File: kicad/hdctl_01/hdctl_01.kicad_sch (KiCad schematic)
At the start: 15 parts, among them J1 DIN41612_02x32_AC, J2 Conn_02x20_Odd_Even, SW1 SW_DIP_x04, U1 PAL20RS10, U2 74HCT574, U3 74HCT574, U4 74HC245, U5 74HC193

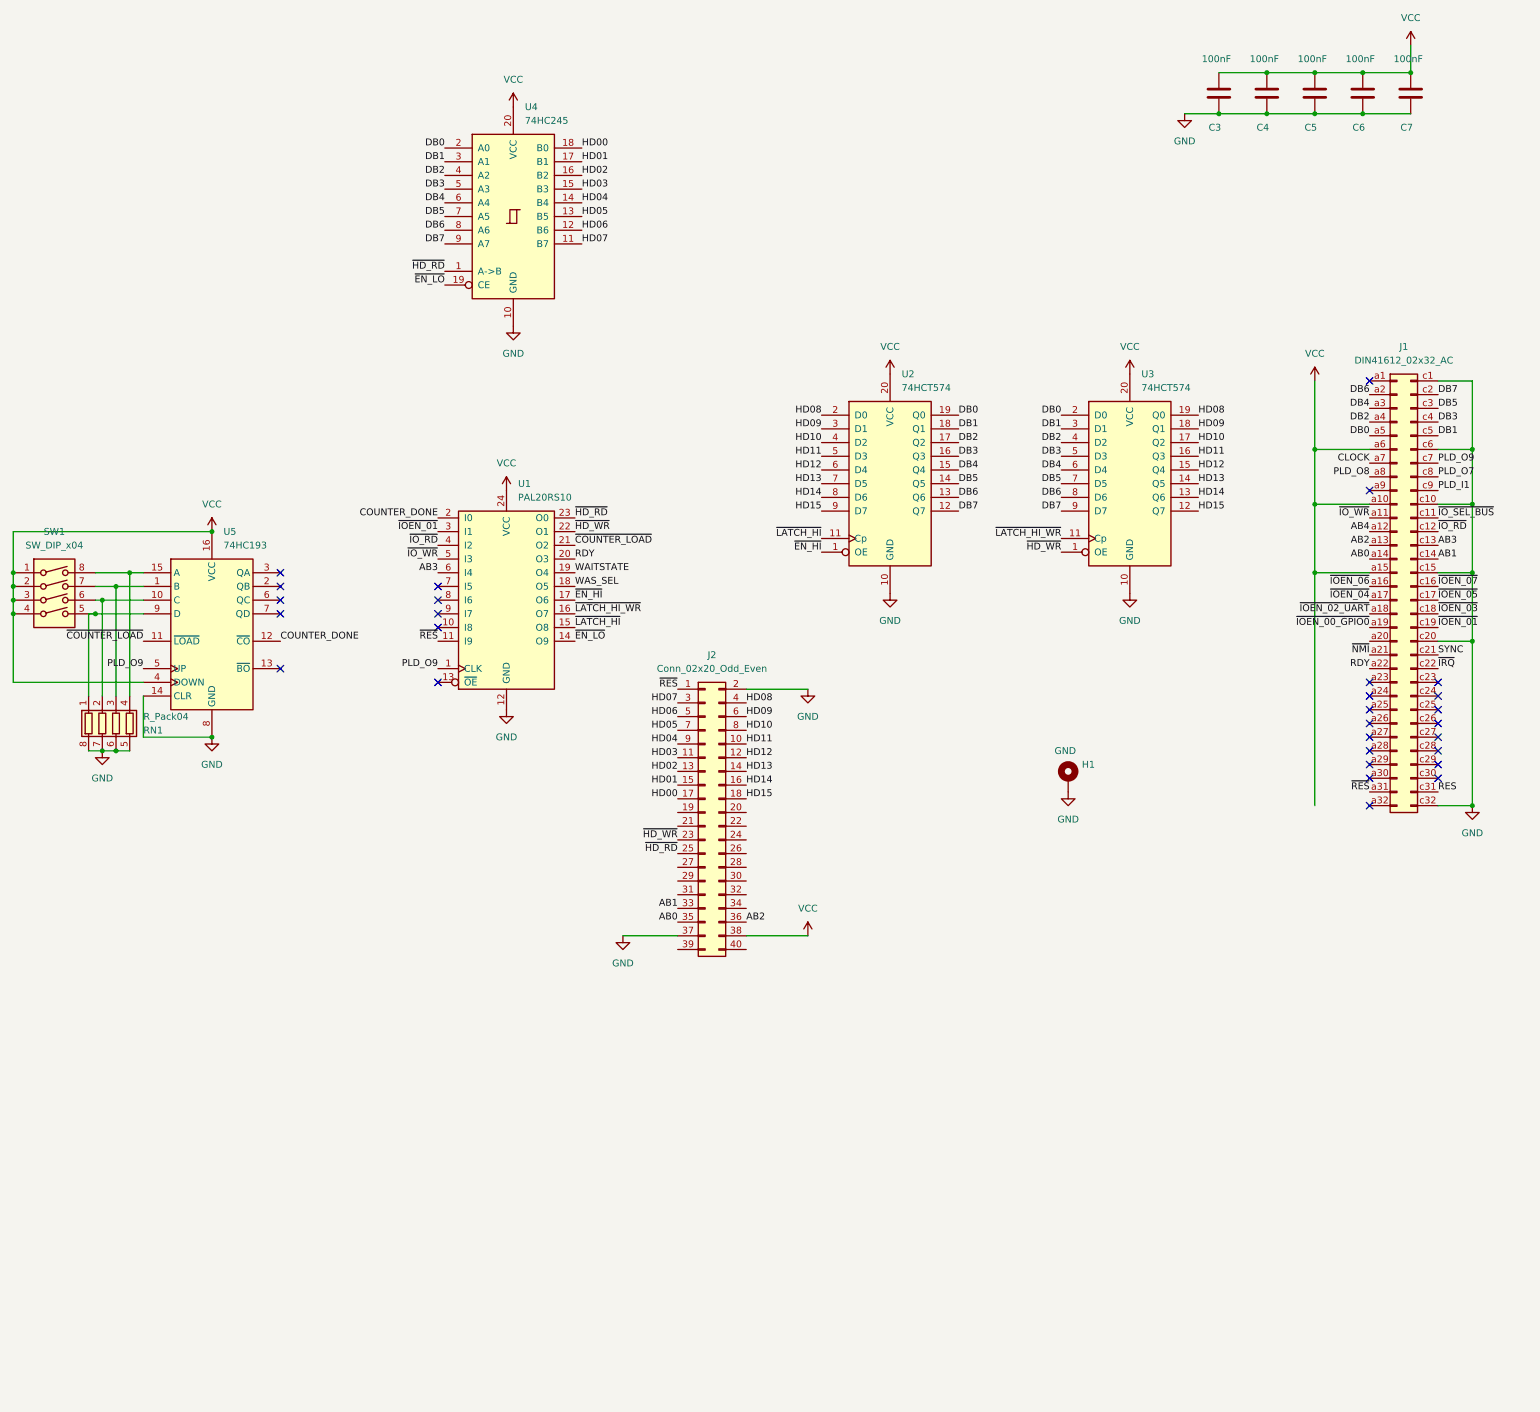
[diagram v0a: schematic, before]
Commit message: hd controller rework. should be ready for mfg (need final check)
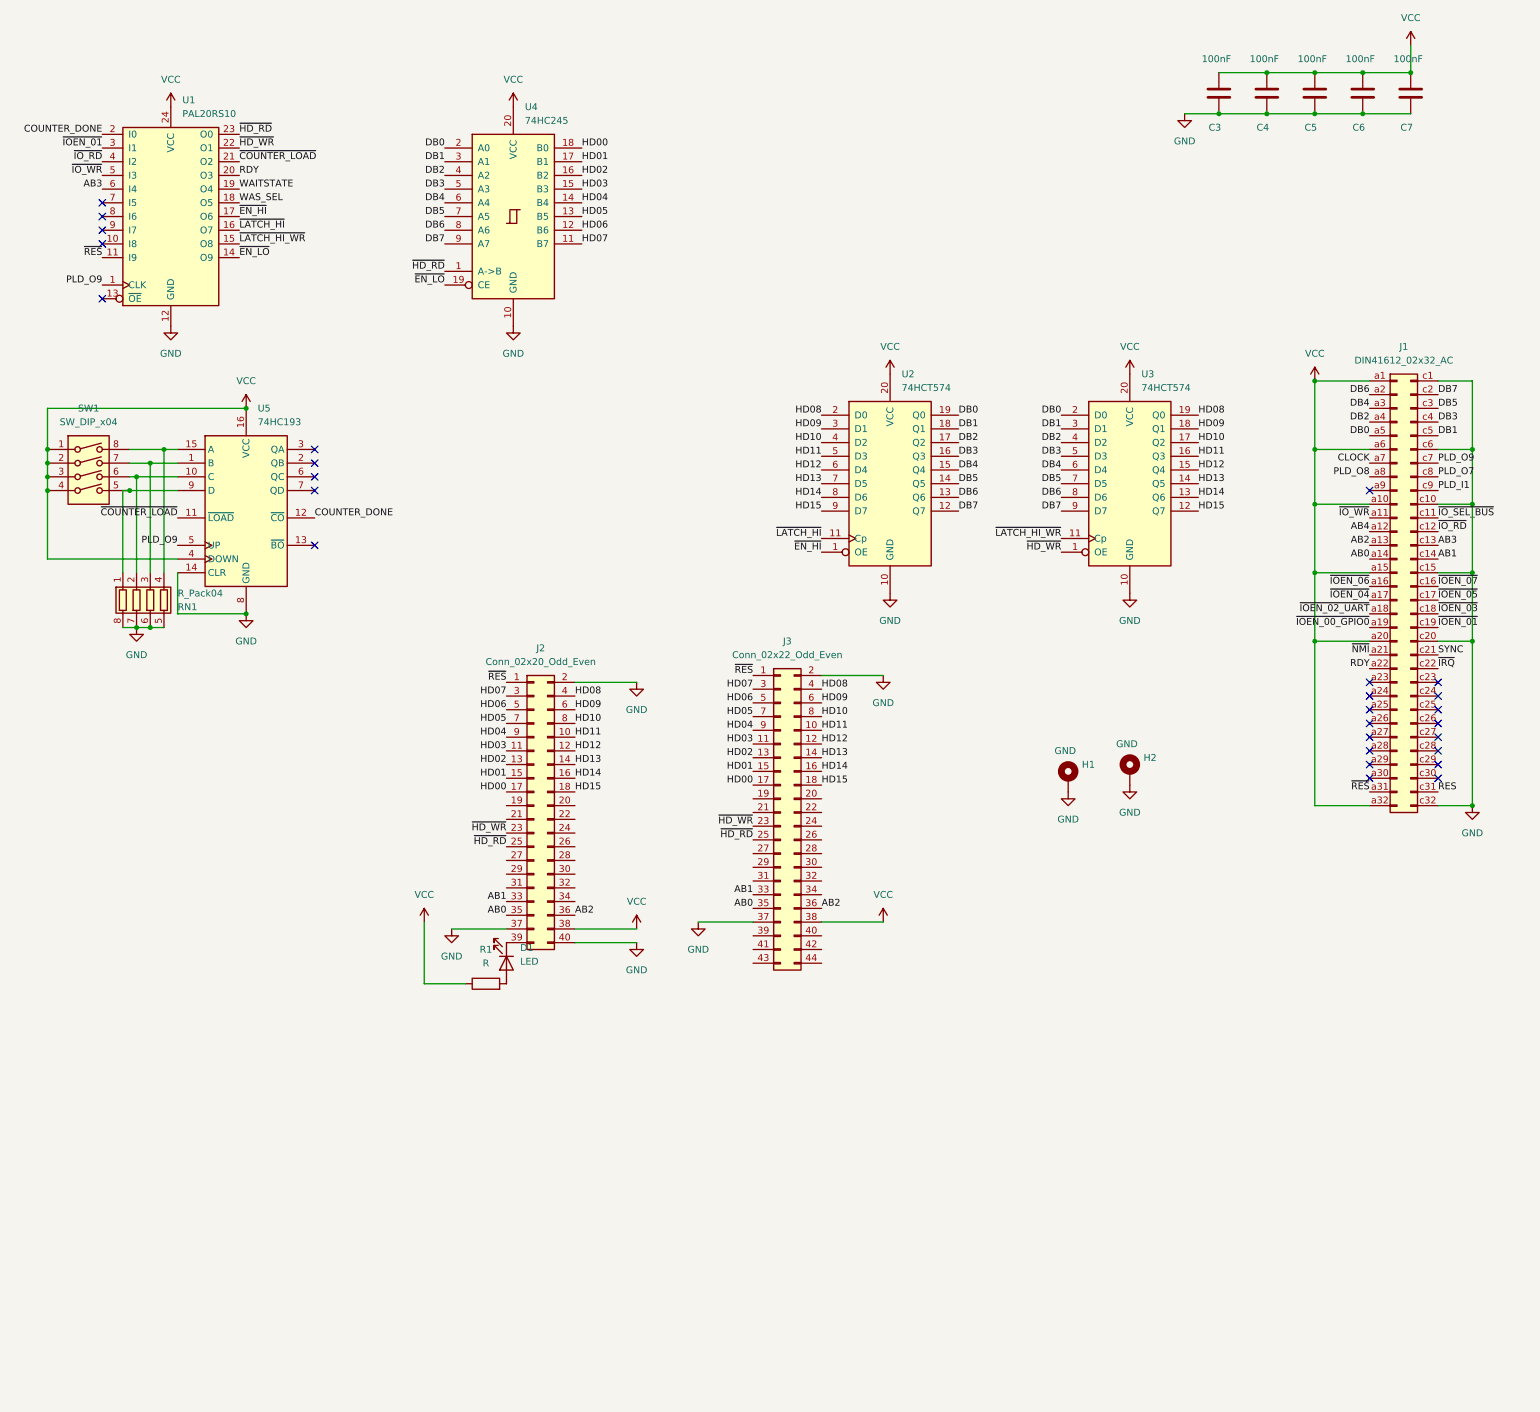
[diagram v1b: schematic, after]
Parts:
- added D1: LED, LED_SMD:LED_0805_2012Metric_Pad1.15x1.40mm_HandSolder, symbol Device:LED
- added H2: GND, MountingHole:MountingHole_3.2mm_M3_DIN965_Pad, symbol Mechanical:MountingHole_Pad
- added J3: Conn_02x22_Odd_Even, Connector_PinSocket_2.00mm:PinSocket_2x22_P2.00mm_Horizontal, symbol Connector_Generic:Conn_02x22_Odd_Even
- added R1: R, Resistor_SMD:R_0805_2012Metric_Pad1.20x1.40mm_HandSolder, symbol Device:R
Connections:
- net AB0: now also J3.35 (Pin_35)
- net AB1: now also J3.33 (Pin_33)
- net AB2: now also J3.36 (Pin_36)
- net GND: now also J2.40 (Pin_40), H2.1, J3.2 (Pin_2), J3.37 (Pin_37)
- net HD00: now also J3.17 (Pin_17)
- net HD01: now also J3.15 (Pin_15)
- net HD02: now also J3.13 (Pin_13)
- net HD03: now also J3.11 (Pin_11)
- net HD04: now also J3.9 (Pin_9)
- net HD05: now also J3.7 (Pin_7)
- net HD06: now also J3.5 (Pin_5)
- net HD07: now also J3.3 (Pin_3)
- net HD08: now also J3.4 (Pin_4)
- net HD09: now also J3.6 (Pin_6)
- net HD10: now also J3.8 (Pin_8)
- net HD11: now also J3.10 (Pin_10)
- net HD12: now also J3.12 (Pin_12)
- net HD13: now also J3.14 (Pin_14)
- net HD14: now also J3.16 (Pin_16)
- net HD15: now also J3.18 (Pin_18)
- net VCC: now also J1.a1 (Pin_a1), J1.a20 (Pin_a20), J1.a32 (Pin_a32), J3.38 (Pin_38), R1.1
- net ~{HD_RD}: now also J3.25 (Pin_25)
- net ~{HD_WR}: now also J3.23 (Pin_23)
- net ~{LATCH_HI_WR}: now also U1.15 (O8); no longer U1.16 (O7)
- net ~{LATCH_HI}: now also U1.16 (O7); no longer U1.15 (O8)
- net ~{RES}: now also J3.1 (Pin_1)
- net at J2.39 (Pin_39): now also D1.1 (K)
- new net: D1.2 (A), R1.2
- no-connect marks 29 -> 27
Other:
- moved on the sheet: J2, RN1, SW1, U1, U5

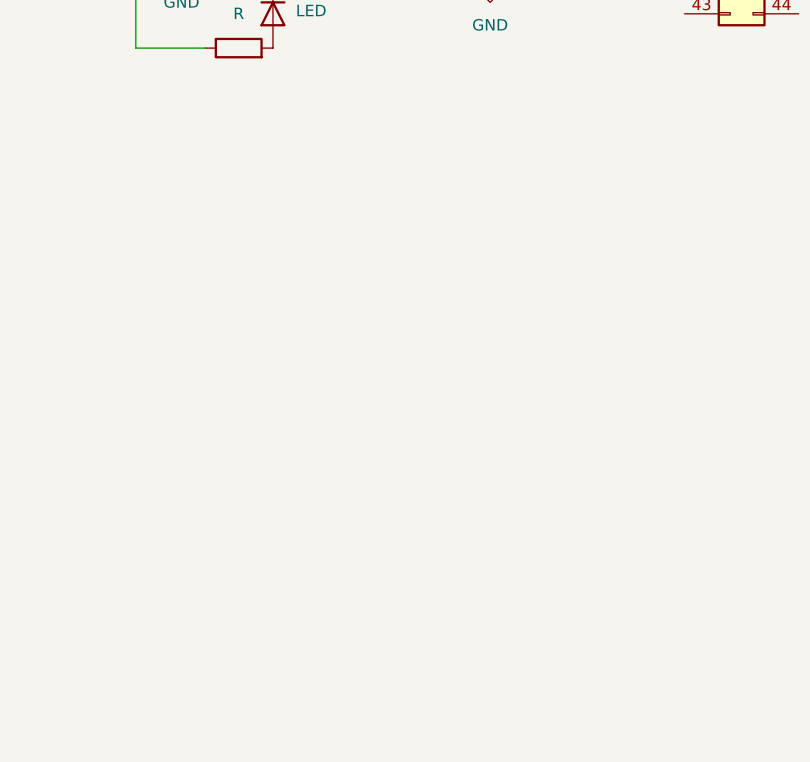
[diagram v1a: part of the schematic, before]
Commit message: added port on the side
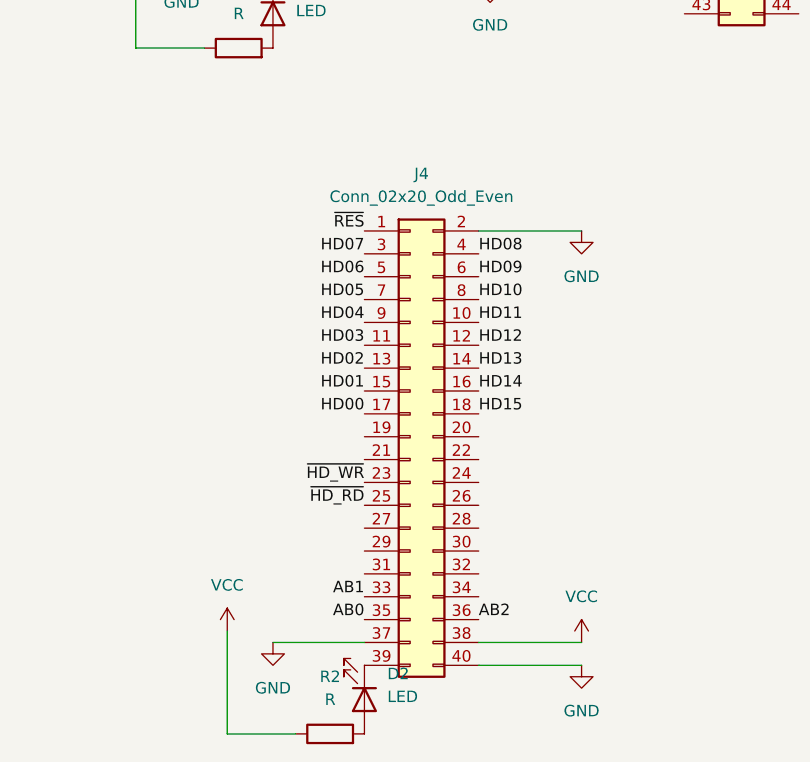
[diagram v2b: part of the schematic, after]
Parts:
- added D2: LED, LED_SMD:LED_0805_2012Metric_Pad1.15x1.40mm_HandSolder, symbol Device:LED
- added J4: Conn_02x20_Odd_Even, Connector_PinHeader_2.54mm:PinHeader_2x20_P2.54mm_Vertical, symbol Connector_Generic:Conn_02x20_Odd_Even
- added R2: R, Resistor_SMD:R_0805_2012Metric_Pad1.20x1.40mm_HandSolder, symbol Device:R
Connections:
- net AB0: now also J4.35 (Pin_35)
- net AB1: now also J4.33 (Pin_33)
- net AB2: now also J4.36 (Pin_36)
- net GND: now also J4.2 (Pin_2), J4.37 (Pin_37), J4.40 (Pin_40)
- net HD00: now also J4.17 (Pin_17)
- net HD01: now also J4.15 (Pin_15)
- net HD02: now also J4.13 (Pin_13)
- net HD03: now also J4.11 (Pin_11)
- net HD04: now also J4.9 (Pin_9)
- net HD05: now also J4.7 (Pin_7)
- net HD06: now also J4.5 (Pin_5)
- net HD07: now also J4.3 (Pin_3)
- net HD08: now also J4.4 (Pin_4)
- net HD09: now also J4.6 (Pin_6)
- net HD10: now also J4.8 (Pin_8)
- net HD11: now also J4.10 (Pin_10)
- net HD12: now also J4.12 (Pin_12)
- net HD13: now also J4.14 (Pin_14)
- net HD14: now also J4.16 (Pin_16)
- net HD15: now also J4.18 (Pin_18)
- net VCC: now also J4.38 (Pin_38), R2.1
- net ~{HD_RD}: now also J4.25 (Pin_25)
- net ~{HD_WR}: now also J4.23 (Pin_23)
- net ~{RES}: now also J4.1 (Pin_1)
- new net: D2.1 (K), J4.39 (Pin_39)
- new net: D2.2 (A), R2.2

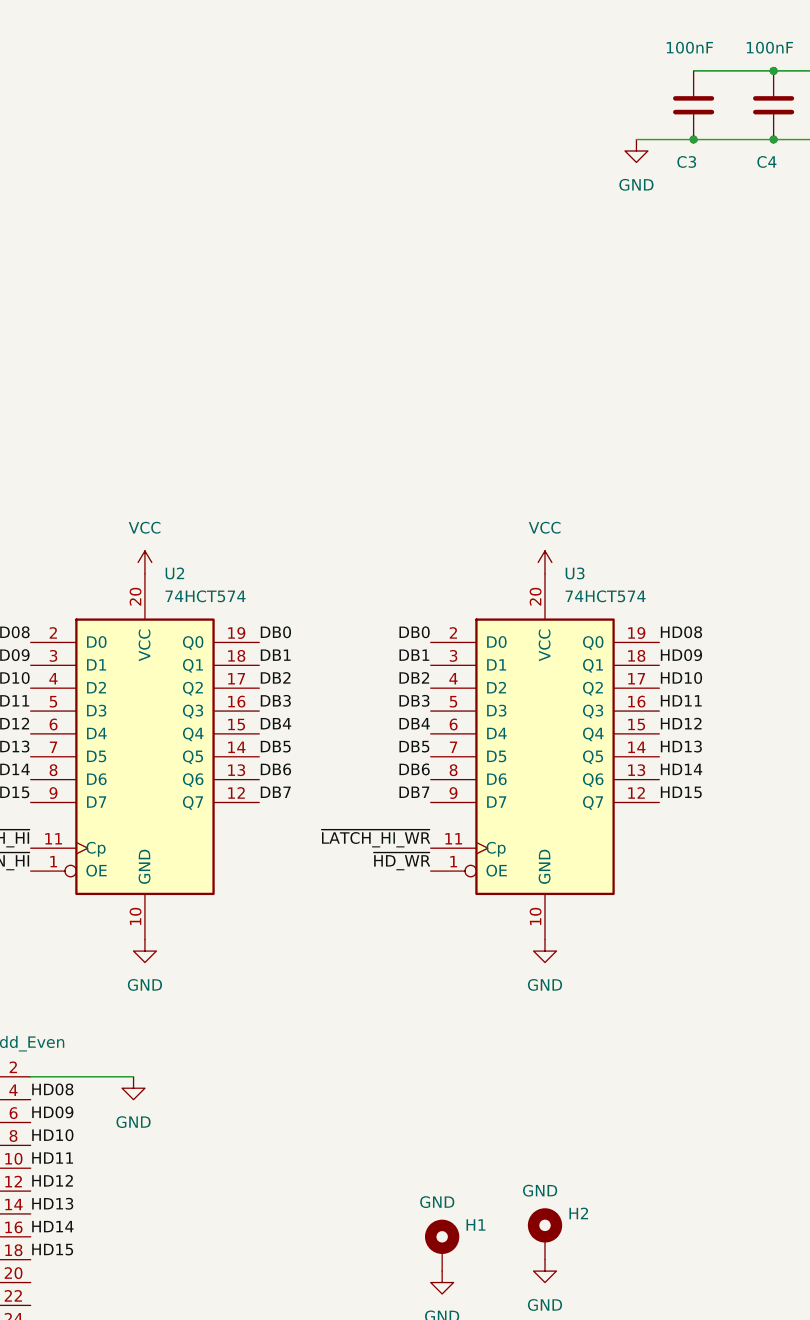
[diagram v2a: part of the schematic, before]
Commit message: hdctl: update PLD pinout to pcb layout, add monting holes to pcb
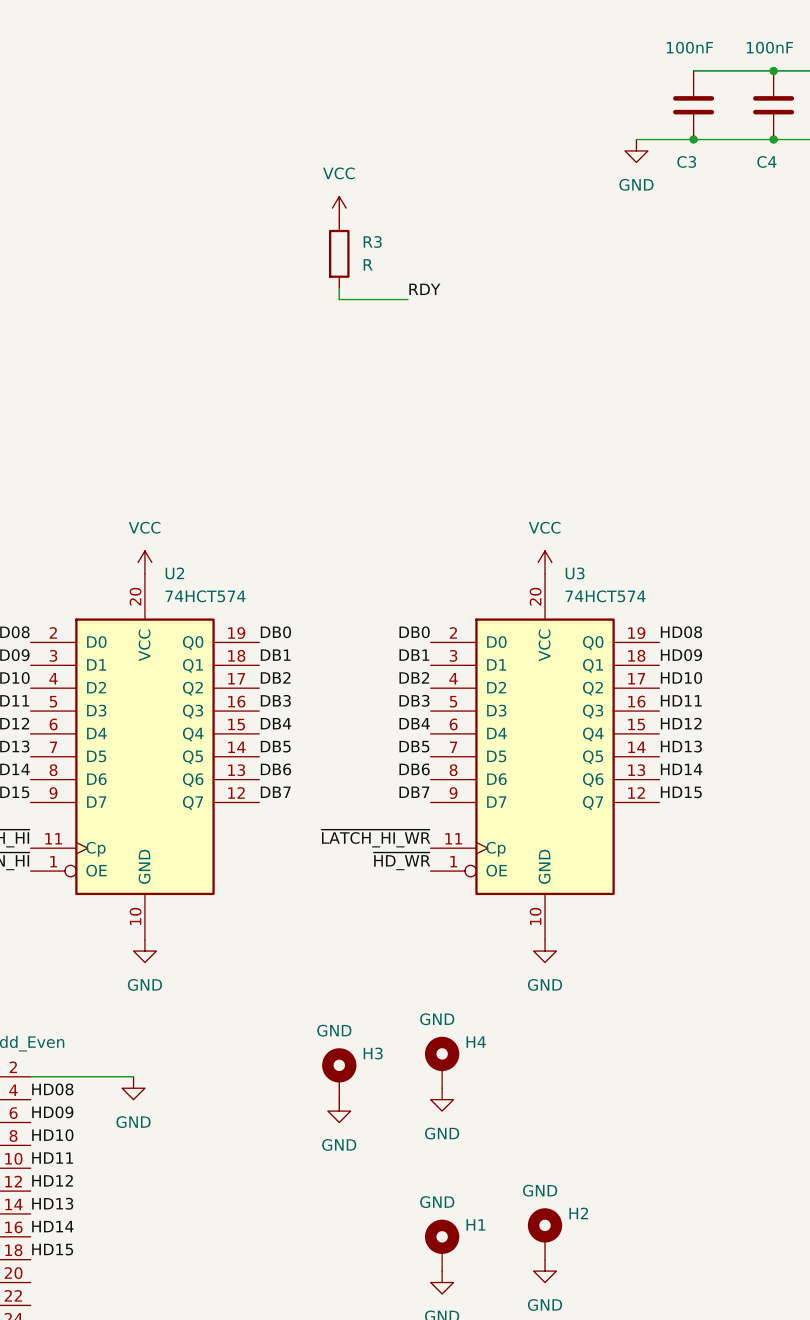
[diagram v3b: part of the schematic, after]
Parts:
- added H3, H4: GND, MountingHole:MountingHole_3.2mm_M3_DIN965_Pad, symbol Mechanical:MountingHole_Pad
- added R3: R, Resistor_THT:R_Axial_DIN0207_L6.3mm_D2.5mm_P7.62mm_Horizontal, symbol Device:R
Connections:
- net GND: now also H3.1, H4.1
- net RDY: now also R3.2
- net VCC: now also R3.1

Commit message: final (?) hdctl pcb layout
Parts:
- added J5: Conn_01x02_Socket, Connector_PinSocket_2.54mm:PinSocket_1x02_P2.54mm_Vertical, symbol Connector:Conn_01x02_Socket
- added JP1: SolderJumper_3_Open, Jumper:SolderJumper-3_P1.3mm_Open_RoundedPad1.0x1.5mm, symbol Jumper:SolderJumper_3_Open
- J2, J4: footprint Connector_PinHeader_2.54mm:PinHeader_2x20_P2.54mm_Vertical -> Connector_IDC:IDC-Header_2x20_P2.54mm_Vertical
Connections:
- net GND: now also J2.19 (Pin_19), J2.22 (Pin_22), J2.24 (Pin_24), J2.26 (Pin_26), J2.30 (Pin_30), J3.19 (Pin_19), J3.22 (Pin_22), J3.24 (Pin_24), J3.26 (Pin_26), J3.30 (Pin_30), J3.40 (Pin_40), J3.43 (Pin_43), J4.19 (Pin_19), J4.22 (Pin_22), J4.24 (Pin_24), J4.26 (Pin_26), J4.30 (Pin_30), J5.1 (Pin_1)
- net VCC: now also J3.41 (Pin_41), JP1.1 (A)
- net VCC_MOT: now reaches J3.42 (Pin_42)
- net VCC_MOT: now also JP1.2 (C)
- new net: J5.2 (Pin_2), JP1.3 (B)
- no-connect marks 27 -> 52
